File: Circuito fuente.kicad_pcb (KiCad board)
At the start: 2 copper layers, 99.1 x 99 mm, 37 parts, among them Q1 TIP122, U1 Bornera_1x3, U2 Bornera_1x2, U3 Bornera_1x3, U35 LM7812_TO220, U39 LM7912_TO220, U4 LM7812_TO220, U40 LM7805_TO220, U41 LM7905_TO220, U45 LD1117S12TR_SOT223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

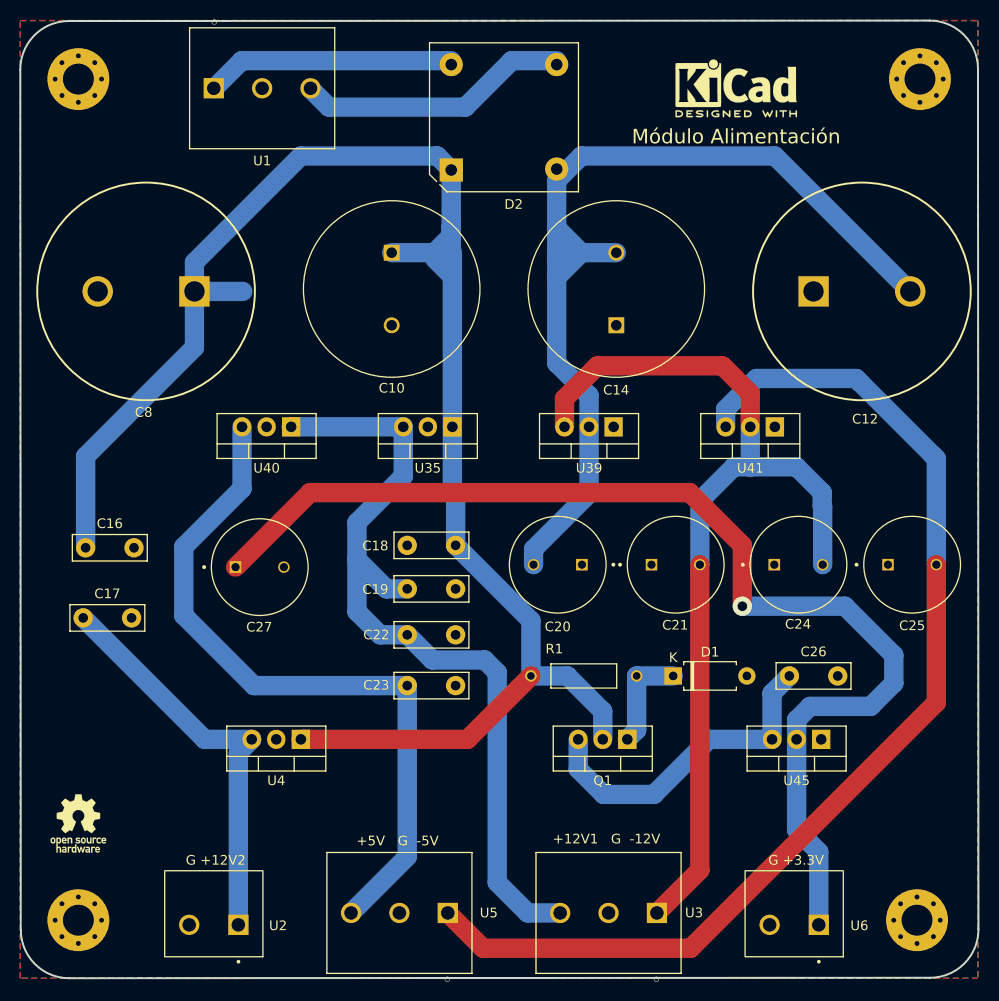
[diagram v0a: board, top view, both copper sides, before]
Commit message: De 2 a 1 Layer + 3D model add
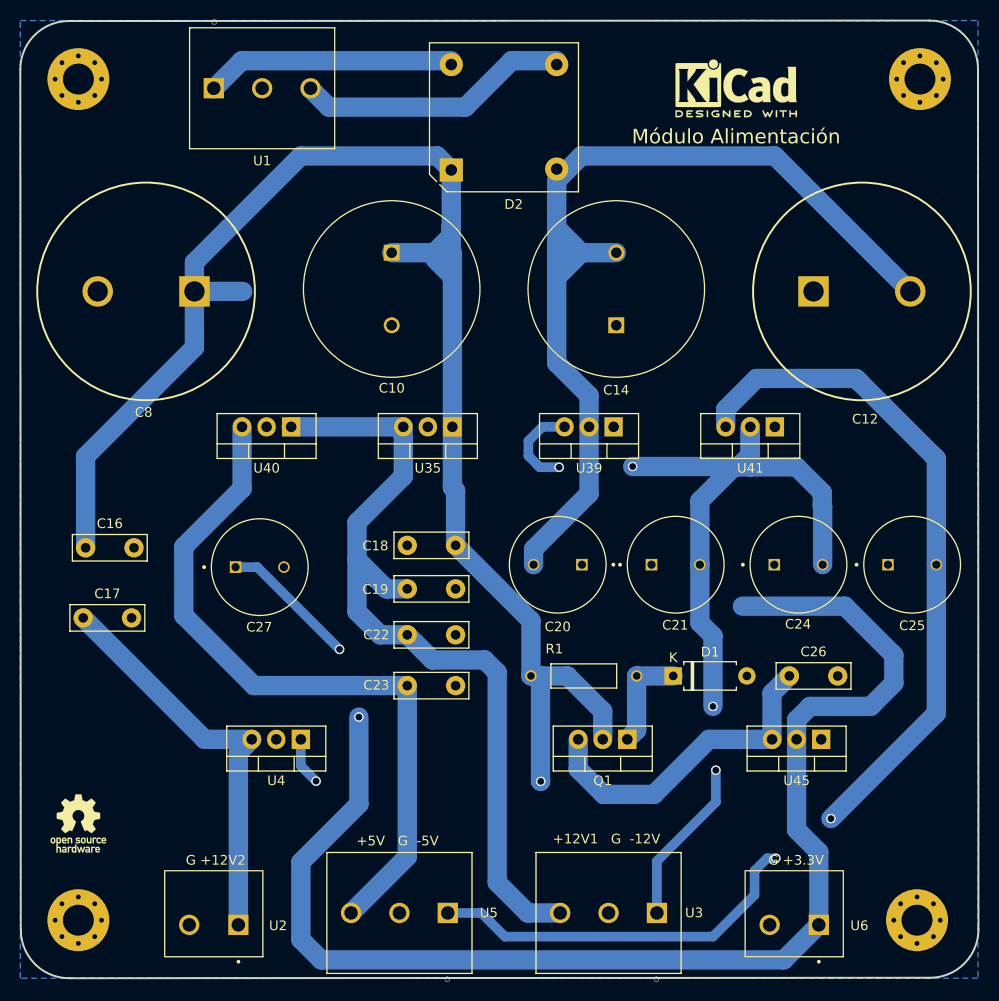
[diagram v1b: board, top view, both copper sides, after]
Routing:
- net /+3,3V: track 118.5 -> 150.1 mm, vias 1 -> 2
- net /+15DC: track 177.0 -> 166.4 mm, vias 0 -> 2
- net /-12V: track 99.4 -> 91.0 mm, vias 0 -> 4
- net /-5V: track 116.1 -> 109.8 mm, vias 0 -> 2
- removed copper zone on F.Cu, net GND
